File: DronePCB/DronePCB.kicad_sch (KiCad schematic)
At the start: 1 part, among them U1 RASPBERRY_PI_ZERO_2_W

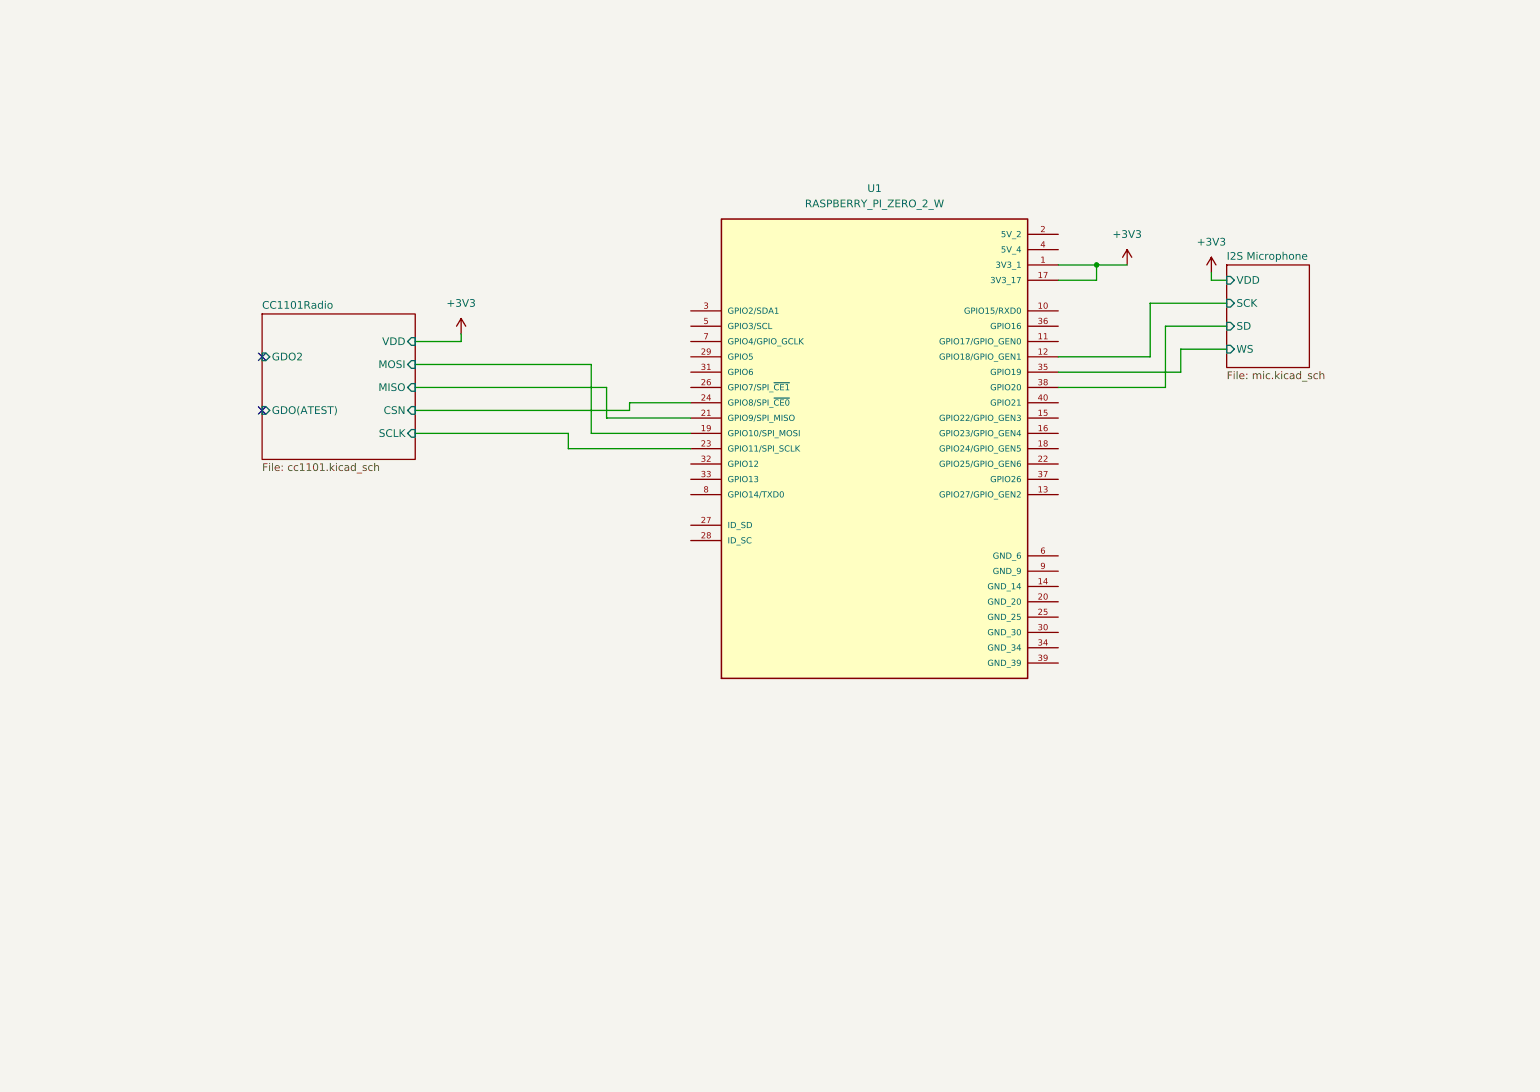
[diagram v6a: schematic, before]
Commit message: Added IR circuit to main schematic | fixed RPi header gnd
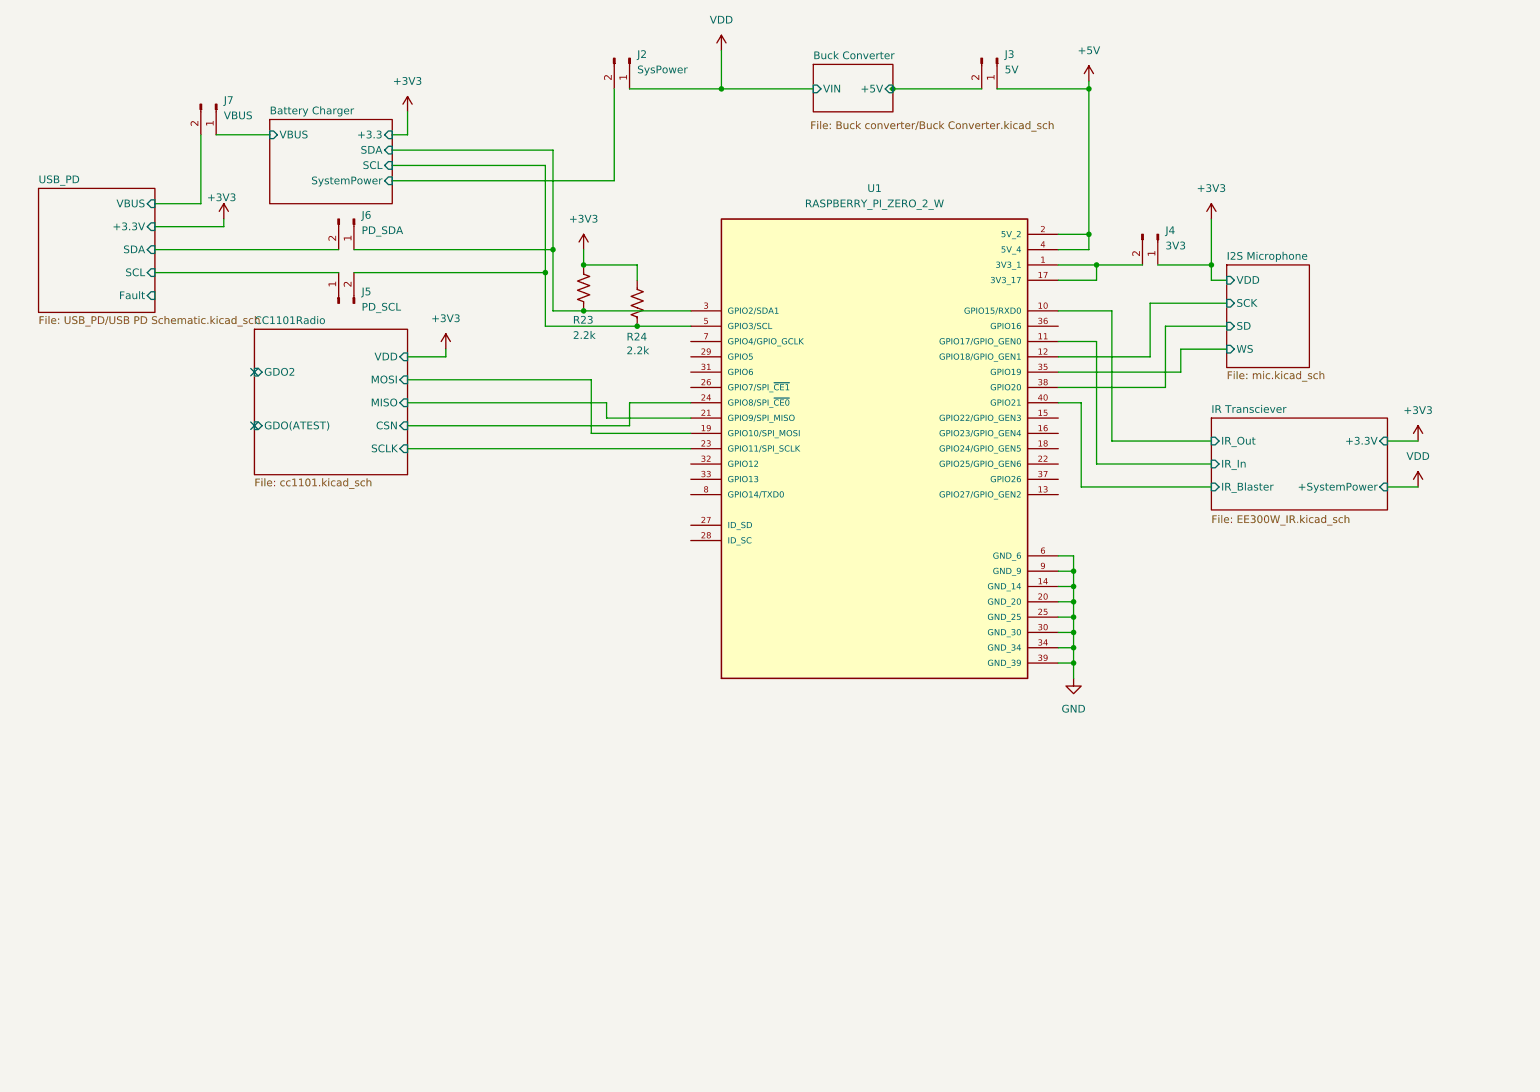
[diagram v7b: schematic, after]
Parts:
- added J2: SysPower, Connector_PinHeader_2.54mm:PinHeader_1x02_P2.54mm_Vertical, symbol Connector:Conn_01x02_Pin
- added J3: 5V, Connector_PinHeader_2.54mm:PinHeader_1x02_P2.54mm_Vertical, symbol Connector:Conn_01x02_Pin
- added J4: 3V3, Connector_PinHeader_2.54mm:PinHeader_1x02_P2.54mm_Vertical, symbol Connector:Conn_01x02_Pin
- added J5: PD_SCL, Connector_PinHeader_2.54mm:PinHeader_1x02_P2.54mm_Vertical, symbol Connector:Conn_01x02_Pin
- added J6: PD_SDA, Connector_PinHeader_2.54mm:PinHeader_1x02_P2.54mm_Vertical, symbol Connector:Conn_01x02_Pin
- added J7: VBUS, Connector_PinHeader_2.54mm:PinHeader_1x02_P2.54mm_Vertical, symbol Connector:Conn_01x02_Pin
- added R23, R24: 2.2k, symbol Device:R_US
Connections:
- net +3V3: now also J4.1 (Pin_1), R23.1, R24.1; no longer U1.1 (3V3_1), U1.17 (3V3_17)
- net IR Transciever/IR_Out: now reaches U1.10 (GPIO15/RXD0)
- net IR Transciever/IR_In: now reaches U1.11 (GPIO17/GPIO_GEN0)
- net GND: now reaches U1.14 (GND_14)
- net GND: now also U1.20 (GND_20), U1.25 (GND_25), U1.30 (GND_30), U1.34 (GND_34), U1.39 (GND_39), U1.6 (GND_6), U1.9 (GND_9)
- net +5V: now reaches U1.2 (5V_2)
- net +5V: now also U1.4 (5V_4), J3.1 (Pin_1)
- net Battery Charger/SDA: now reaches U1.3 (GPIO2/SDA1)
- net Battery Charger/SDA: now also J6.1 (Pin_1), R23.2
- net IR Transciever/IR_Blaster: now reaches U1.40 (GPIO21)
- net Battery Charger/SCL: now reaches U1.5 (GPIO3/SCL)
- net Battery Charger/SCL: now also J5.2 (Pin_2), R24.2
- new net: J4.2 (Pin_2), U1.1 (3V3_1), U1.17 (3V3_17)
- new net Battery Charger/SystemPower: J2.2 (Pin_2)
- new net Battery Charger/VBUS: J7.1 (Pin_1)
- new net Buck Converter/+5V: J3.2 (Pin_2)
- new net USB_PD/SCL: J5.1 (Pin_1)
- new net USB_PD/SDA: J6.2 (Pin_2)
- new net USB_PD/VBUS: J7.2 (Pin_2)
- new net VDD: J2.1 (Pin_1)
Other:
- added sheet Battery Charger (BatteryCharger/Battery_Charger.kicad_sch)
- added sheet Buck Converter (Buck converter/Buck Converter.kicad_sch)
- added sheet IR Transciever (EE300W_IR.kicad_sch)
- added sheet USB_PD (USB_PD/USB PD Schematic.kicad_sch)

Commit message: Completed H-Bridge Circuit | Finished Schematic | Working on pcb design
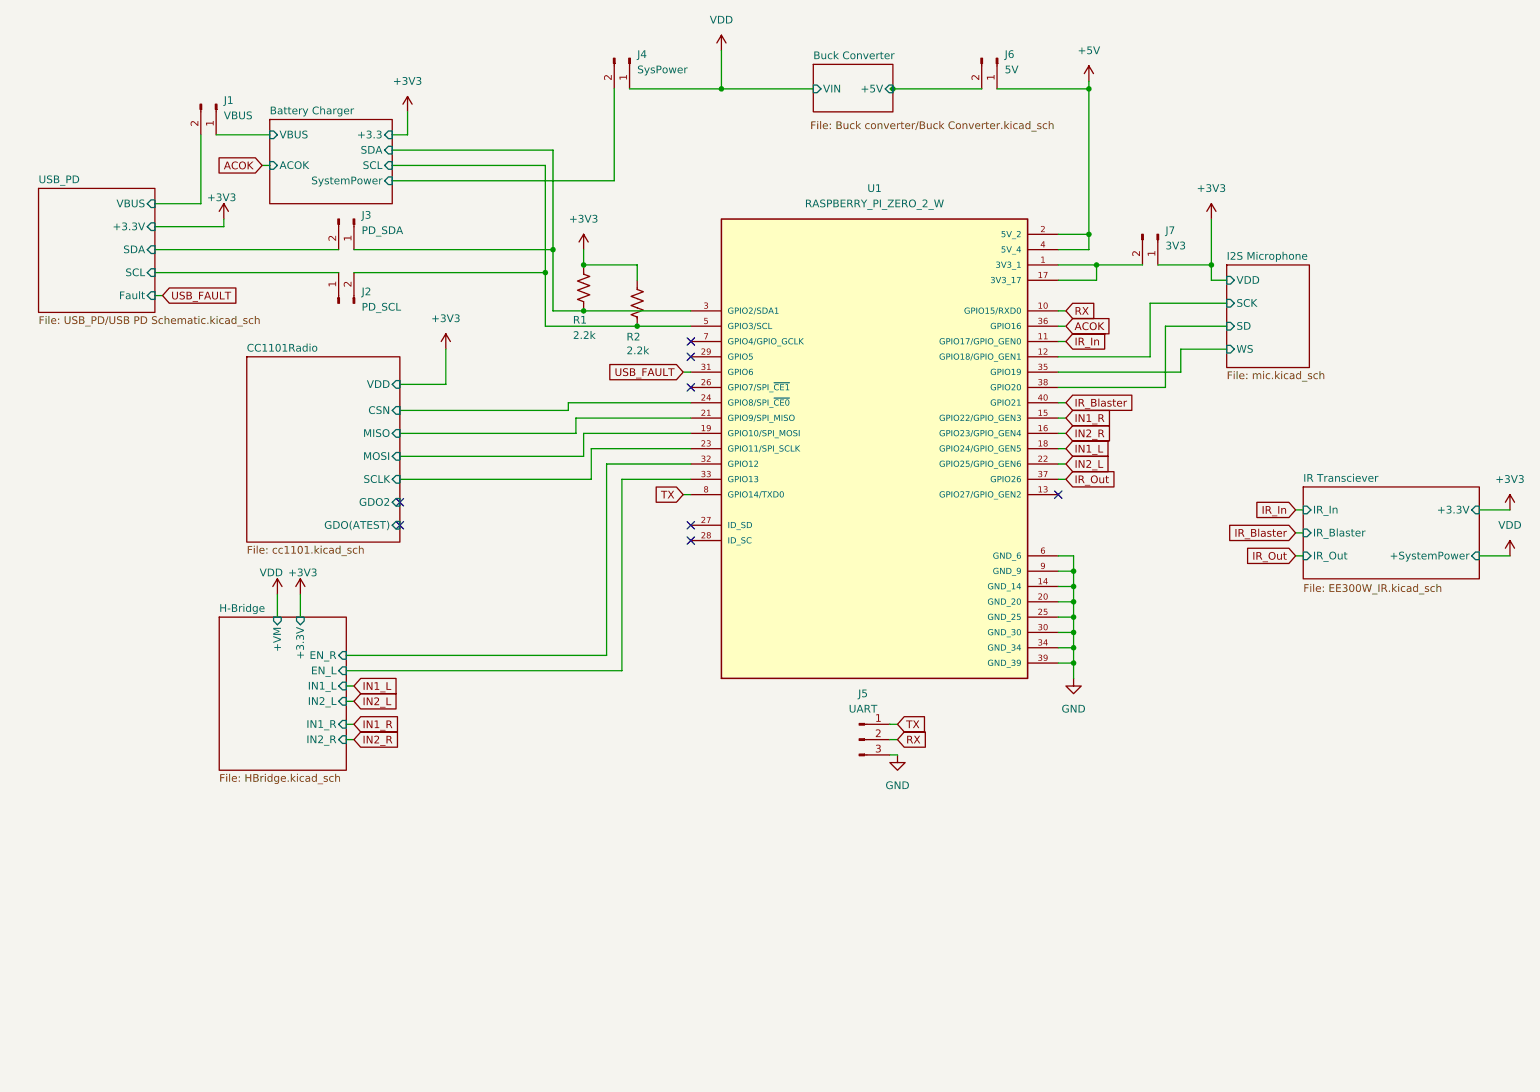
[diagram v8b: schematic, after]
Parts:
- added J5: UART, Connector_PinHeader_2.54mm:PinHeader_1x03_P2.54mm_Vertical, symbol Connector:Conn_01x03_Pin
- R1: renamed from R23; footprint (none) -> Resistor_SMD:R_0603_1608Metric
- R2: renamed from R24; footprint (none) -> Resistor_SMD:R_0603_1608Metric
- renumbered J7 to J1, J5 to J2, J6 to J3, J2 to J4, J3 to J6, J4 to J7
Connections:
- net GND: now also J5.3 (Pin_3)
- net IN1_R: now reaches U1.15 (GPIO22/GPIO_GEN3)
- net IN2_R: now reaches U1.16 (GPIO23/GPIO_GEN4)
- net IN1_L: now reaches U1.18 (GPIO24/GPIO_GEN5)
- net IN2_L: now reaches U1.22 (GPIO25/GPIO_GEN6)
- net USB_FAULT: now reaches U1.31 (GPIO6)
- net H-Bridge/EN_R: now reaches U1.32 (GPIO12)
- net H-Bridge/EN_L: now reaches U1.33 (GPIO13)
- net ACOK: now reaches U1.36 (GPIO16)
- net IR_Out: now reaches U1.37 (GPIO26)
- net TX: now reaches U1.8 (GPIO14/TXD0)
- net TX: now also J5.1 (Pin_1)
- net IR Transciever/IR_Blaster renamed IR_Blaster
- net IR Transciever/IR_In renamed IR_In
- net IR Transciever/IR_Out renamed RX
- net RX: now also J5.2 (Pin_2)
- no-connect marks 2 -> 8
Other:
- added sheet H-Bridge (HBridge.kicad_sch)
- sheet Battery Charger ports: added ACOK; removed none
